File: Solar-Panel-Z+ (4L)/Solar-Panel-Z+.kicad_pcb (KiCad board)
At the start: 4 copper layers, 48.4 x 48.4 mm, 79 parts, among them J1 FTS-105-01-X-DV-A, Q1 NX3008NBKS, Q2 MBT2222ADW1T1, Q3 NX3008NBKS, Q4 MBT2222ADW1T1, U1 BQ25570RGRR, U2 OPT3001, U3 MAX40200AUK

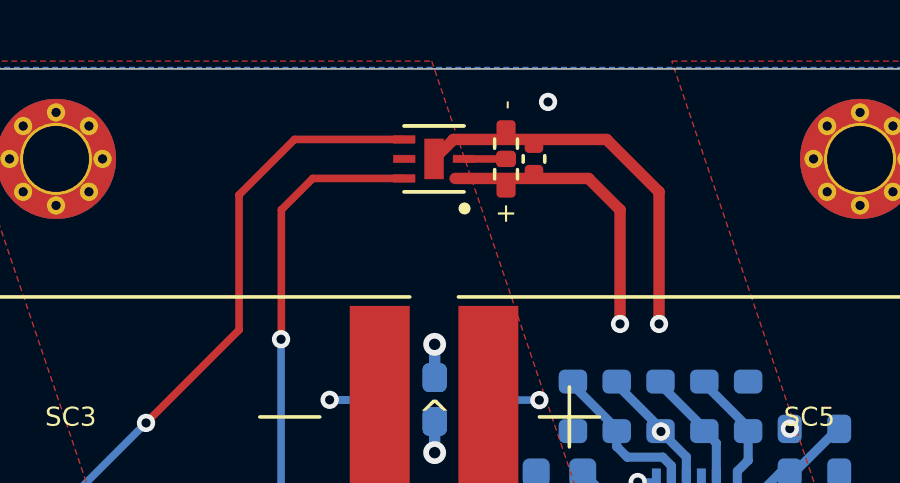
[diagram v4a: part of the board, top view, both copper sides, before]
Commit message: Updated Sun Sensor to OPT4001
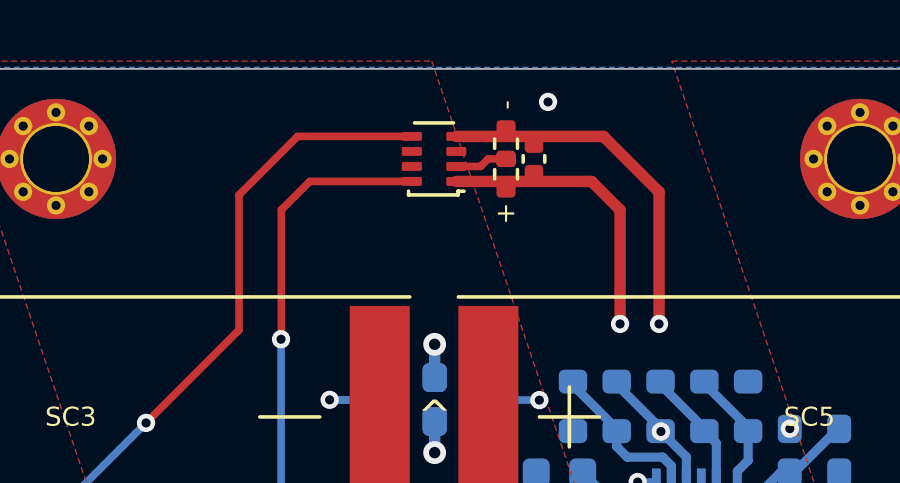
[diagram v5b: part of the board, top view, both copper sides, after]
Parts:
- U2: value OPT3001 -> OPT4001; footprint solarpanels:OPT3001 -> Package_TO_SOT_SMD:SOT-583-8
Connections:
- U2 pad 3: GND -> unconnected-(U2-NC-Pad3)
- U2 pad 4: SCL_LS -> GND
- U2 pad 5: unconnected-(U2-INT-Pad5) -> SCL_LS
- U2 pad 6: SDA_LS -> unconnected-(U2-NC-Pad6)
- U2 pad 7: GND -> unconnected-(U2-INT-Pad7)
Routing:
- net GND: track 23.1 -> 22.1 mm

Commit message: Updated Rev to B3/03
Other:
- board text added: "Rev B3/03"
- board text removed: "Rev B3/02"
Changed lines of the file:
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@@
     (effects (font (size 0.635 0.635) (thickness 0.127)))
   )
-  (gr_text "Rev B3/02" (at 105.825 46.665) (layer "B.Mask")
+  (gr_text "Rev B3/03" (at 105.825 46.665) (layer "B.Mask")
     (effects (font (size 0.635 0.635) (thickness 0.1524)) (justify mirror))
   )
